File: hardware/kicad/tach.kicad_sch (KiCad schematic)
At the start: 9 parts, among them U301 H11L1

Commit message: Translate code, hardware and docs to English; bilingual dashboard
- tdm-logic i18n module: every dashboard text in English and Italian,
  chosen by `[display] language` in the profile (English by default, the
  TDM 850 profile keeps Italian); number formatting per language
- Slint fixed labels moved to a `Labels` global filled from the same table;
  `tdm-dash --language en|it`; reference screens regenerated in English with
  Italian check screens
- tdmctl, tdm-dash CLI, simulator scenarios, calibration errors and tools
  print English
- KiCad sheets, WireViz harnesses, perfboard plan and CAD comments in
  English, exports regenerated with the new names
- manual, research, ADRs and READMEs translated; files renamed (docs/manual,
  docs/research, English chapter and ADR names); status markers are now
  [VERIFIED] / [TO VERIFY] / [HYPOTHESIS]

Co-Authored-By: Claude Opus 5.5 <noreply@anthropic.com>
Claude-Session: https://claude.ai/code/session_01G9D4Wshjz9MkaThp4wsrGP
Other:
- note added: "IGN → GP3, active low"
- note added: "Tachometer"
- note added: "The coil negative has spikes of a few hundred volts at every spark. 1N4007 passes only the positive ones, 2 × 22 kΩ 1 W limit the current, the 15 V zener and the 2.2 nF clip the spike; the H11L1 (Schmitt trigger) gives a clean edge. Tachometer wire and waveform [TO VERIFY] with the oscilloscope."
- note removed: "Contagiri"
- note removed: "IGN → GP3, attivo basso"
- note removed: "Il negativo della bobina ha picchi di alcune centinaia di volt a ogni scintilla. 1N4007 lascia passare solo i positivi, 2 × 22 kΩ 1 W limitano la corrente, lo zener da 15 V e il 2,2 nF tagliano il picco; l'H11L1 (trigger di Schmitt) dà un fronte pulito. Filo del contagiri e forma d'onda [DA VERIFICARE] con l'oscilloscopio."
- title: Contagiri (negativo bobina) -> Tachometer (coil negative)
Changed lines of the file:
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@@
 	(paper "A4")
 	(title_block
-		(title "Contagiri (negativo bobina)")
+		(title "Tachometer (coil negative)")
 		(date "2026-10-21")
 		(rev "0.1")
 		(company "tdm-dash · CERN-OHL-P-2.0")
-		(comment 1 "Foglio 3 di 8")
-		(comment 2 "Generato da hardware/kicad/generate.py: non modificare a mano")
+		(comment 1 "Sheet 3 of 8")
+		(comment 2 "Generated by hardware/kicad/generate.py: do not edit by hand")
 	)
 	(symbol
@@
 		)
 	)
-	(text "Contagiri"
+	(text "Tachometer"
 		(exclude_from_sim no)
 		(at 10.16 12.7 0)
@@
 		)
 	)
-	(text "Il negativo della bobina ha picchi di alcune centinaia di volt a ogni scintilla.\n1N4007 lascia passare solo i positivi, 2 × 22 kΩ 1 W limitano la corrente, lo zener\nda 15 V e il 2,2 nF tagliano il picco; l'H11L1 (trigger di Schmitt) dà un fronte pulito.\nFilo del contagiri e forma d'onda [DA VERIFICARE] con l'oscilloscopio."
+	(text "The coil negative has spikes of a few hundred volts at every spark.\n1N4007 passes only the positive ones, 2 × 22 kΩ 1 W limit the current, the 15 V\nzener and the 2.2 nF clip the spike; the H11L1 (Schmitt trigger) gives a clean edge.\nTachometer wire and waveform [TO VERIFY] with the oscilloscope."
 		(exclude_from_sim no)
 		(at 10.16 17.78 0)
@@
 		)
 	)
-	(text "IGN → GP3, attivo basso"
+	(text "IGN → GP3, active low"
 		(exclude_from_sim no)
 		(at 215.9 88.9 0)

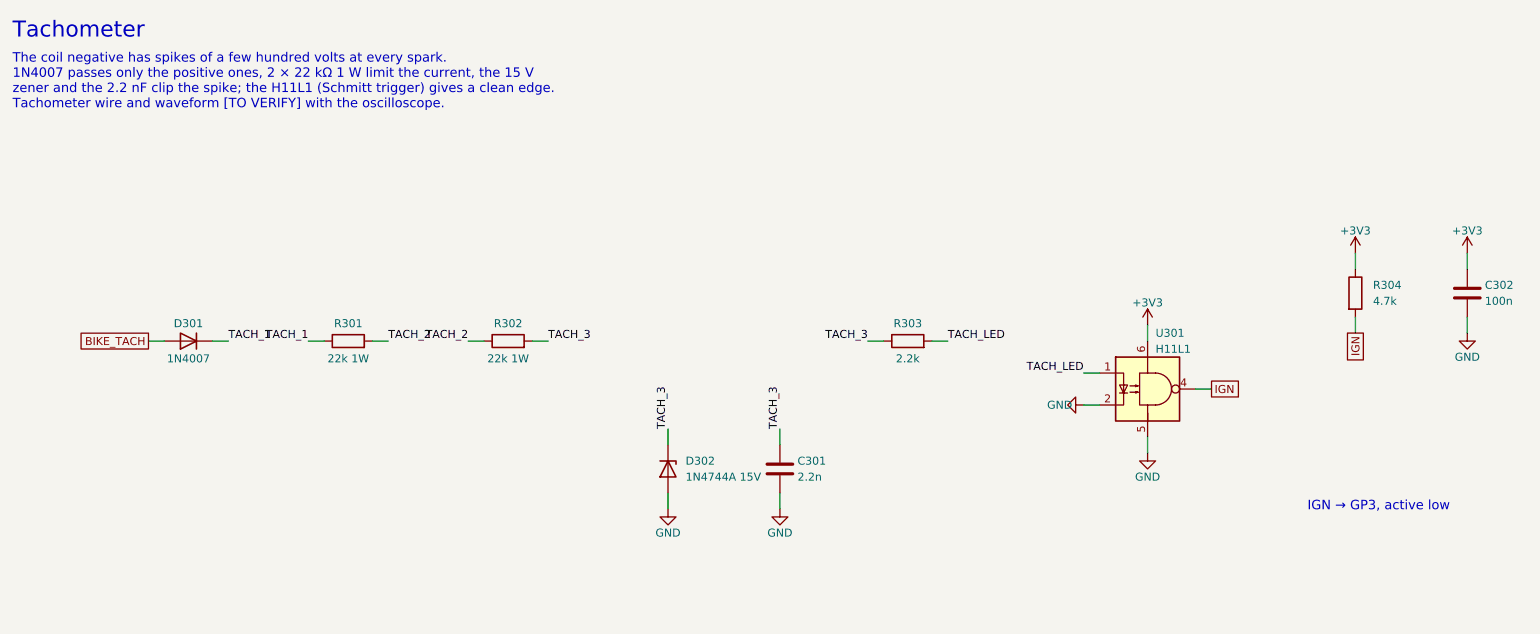
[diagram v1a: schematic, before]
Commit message: Schematic: drawn wires, block diagram, new title block
The sheets were a netlist in disguise: every pin ended in a short stub and
a label, so the circuits had to be pieced together by name, labels
overlapped, two sheets fell off the index page and the title block was
KiCad's default. The generator now draws the schematic:

- hardware/kicad/schgen: placement on the 50 mil grid, orthogonal wires,
  junctions, hierarchical ports, module and connector symbols with named
  pins; the drawing is normalised the way KiCad 9 reads it and checked
  against the declared netlist (no wire may connect anything else)
- hardware/kicad/sheets: one module per sheet, laid out left to right
  from the bike to the Pico; the root sheet is a block diagram whose
  wires are the signals between sheets
- tdm-dash.kicad_wks: frame and title block of the project
- symbols copied from KiCad 9.0.9 (vendor_symbols.py): the generator no
  longer needs KiCad installed
- export.sh: ERC, tools/check_netlist.py (KiCad's netlist is the declared
  one), check_pinmap.py, PDF and SVG on white, tools/check_svg_layout.py
  (no text over another text, a wire, the frame or the title block)

The circuit is unchanged: KiCad's netlist of the old and new schematic
has the same 56 nets (FRAM pins now follow the breakout header, R603/R604
pins swapped).

Co-Authored-By: Claude Opus 5.5 <noreply@anthropic.com>
Claude-Session: https://claude.ai/code/session_01G9D4Wshjz9MkaThp4wsrGP
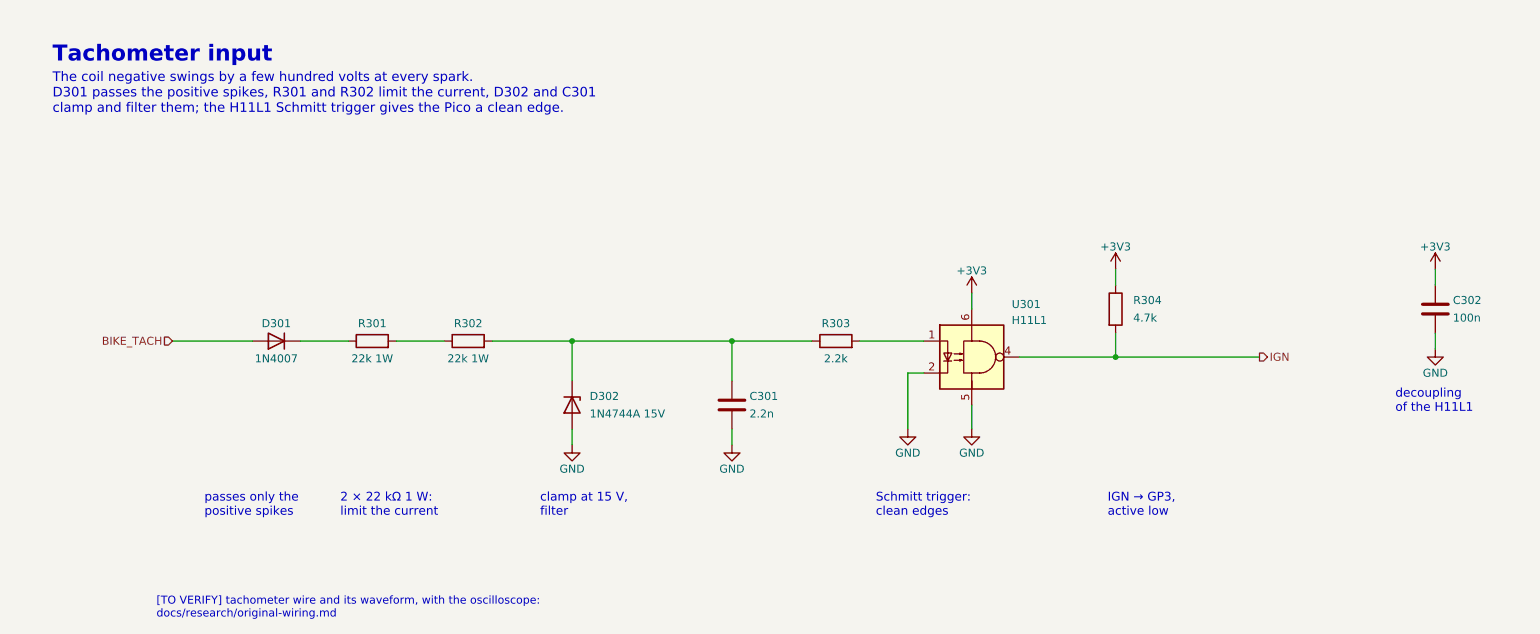
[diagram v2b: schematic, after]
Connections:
- net TACH_1: no longer names the net of D301.1 (K), R301.1
- net TACH_2: no longer names the net of R301.2, R302.1
- net TACH_3: no longer names the net of C301.1, D302.1 (K), R302.2, R303.1
- net TACH_LED: no longer names the net of R303.2, U301.1
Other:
- note added: "2 × 22 kΩ 1 W: limit the current"
- note added: "Schmitt trigger: clean edges"
- note added: "Tachometer input"
- note added: "The coil negative swings by a few hundred volts at every spark. D301 passes the positive spikes, R301 and R302 limit the current, D302 and C301 clamp and filter them; the H11L1 Schmitt trigger gives the Pico a clean edge."
- note added: "[TO VERIFY] tachometer wire and its waveform, with the oscilloscope: docs/research/original-wiring.md"
- note added: "clamp at 15 V, filter"
- note added: "decoupling of the H11L1"
- note added: "passes only the positive spikes"
- note removed: "Tachometer"
- note removed: "The coil negative has spikes of a few hundred volts at every spark. 1N4007 passes only the positive ones, 2 × 22 kΩ 1 W limit the current, the 15 V zener and the 2.2 nF clip the spike; the H11L1 (Schmitt trigger) gives a clean edge. Tachometer wire and waveform [TO VERIFY] with the oscilloscope."
- company: tdm-dash · CERN-OHL-P-2.0 -> tdm-dash
